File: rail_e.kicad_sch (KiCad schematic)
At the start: 49 parts

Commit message: PCBA prototype order
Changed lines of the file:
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@@
-	)
-	(junction
-		(at 279.4 123.19)
-		(diameter 0)
-		(color 0 0 0 0)
 	)
 	(junction
@@
 		)
 		(stroke
-			(width 0)
-			(type default)
-		)
-	)
-	(wire
-		(pts
-			(xy 279.4 123.19) (xy 279.4 147.32)
-		)
-		(stroke

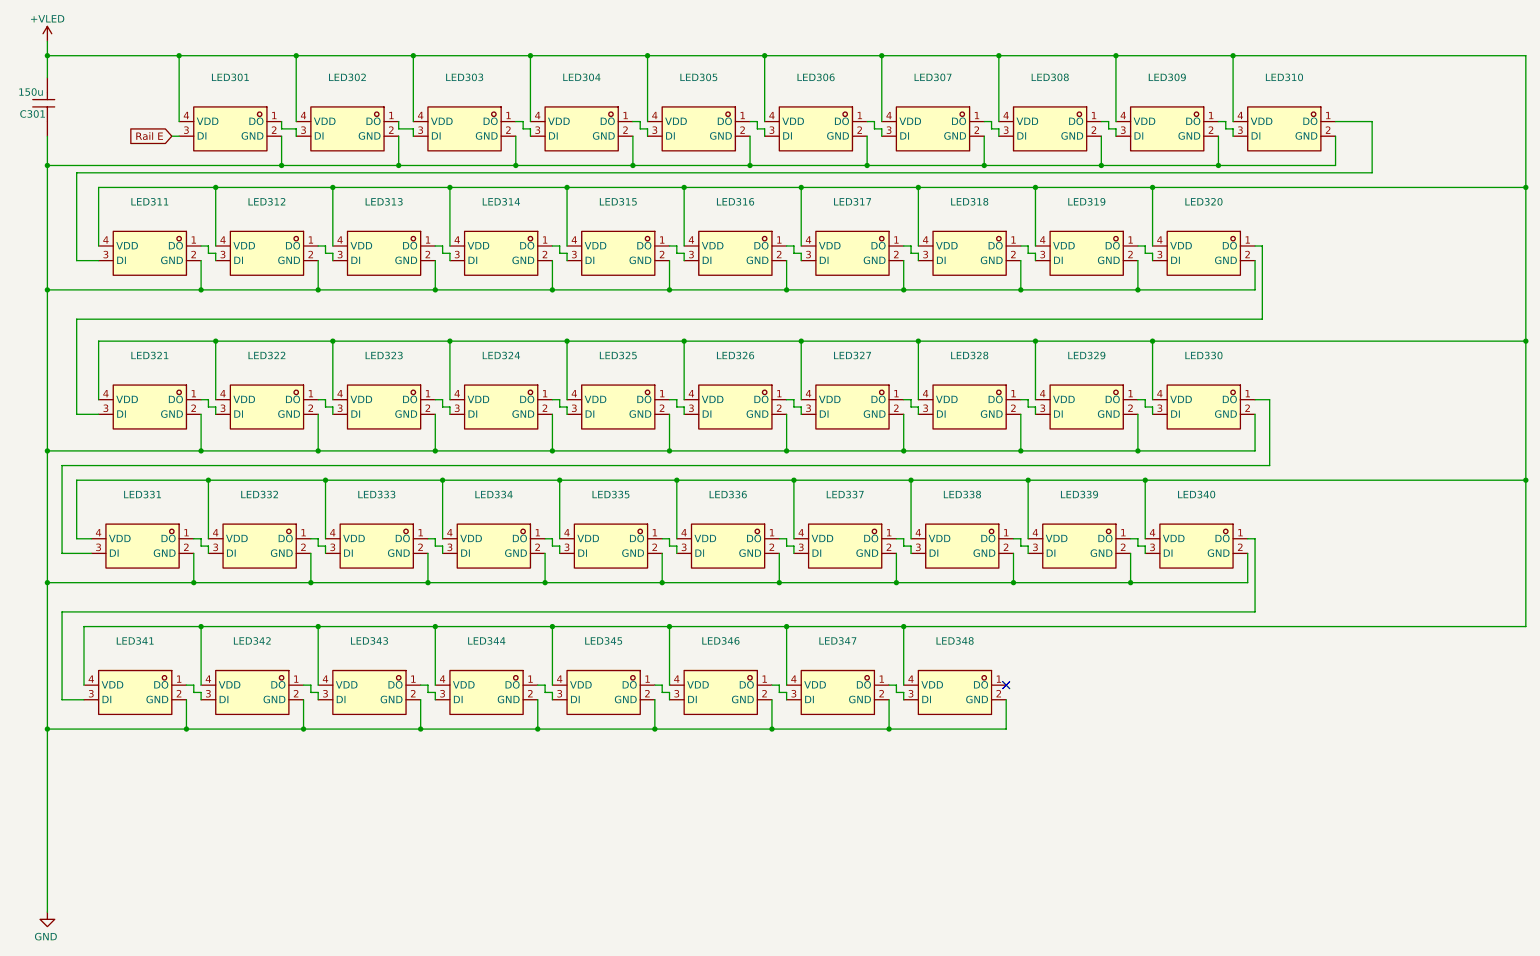
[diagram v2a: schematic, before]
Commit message: Add rail labels
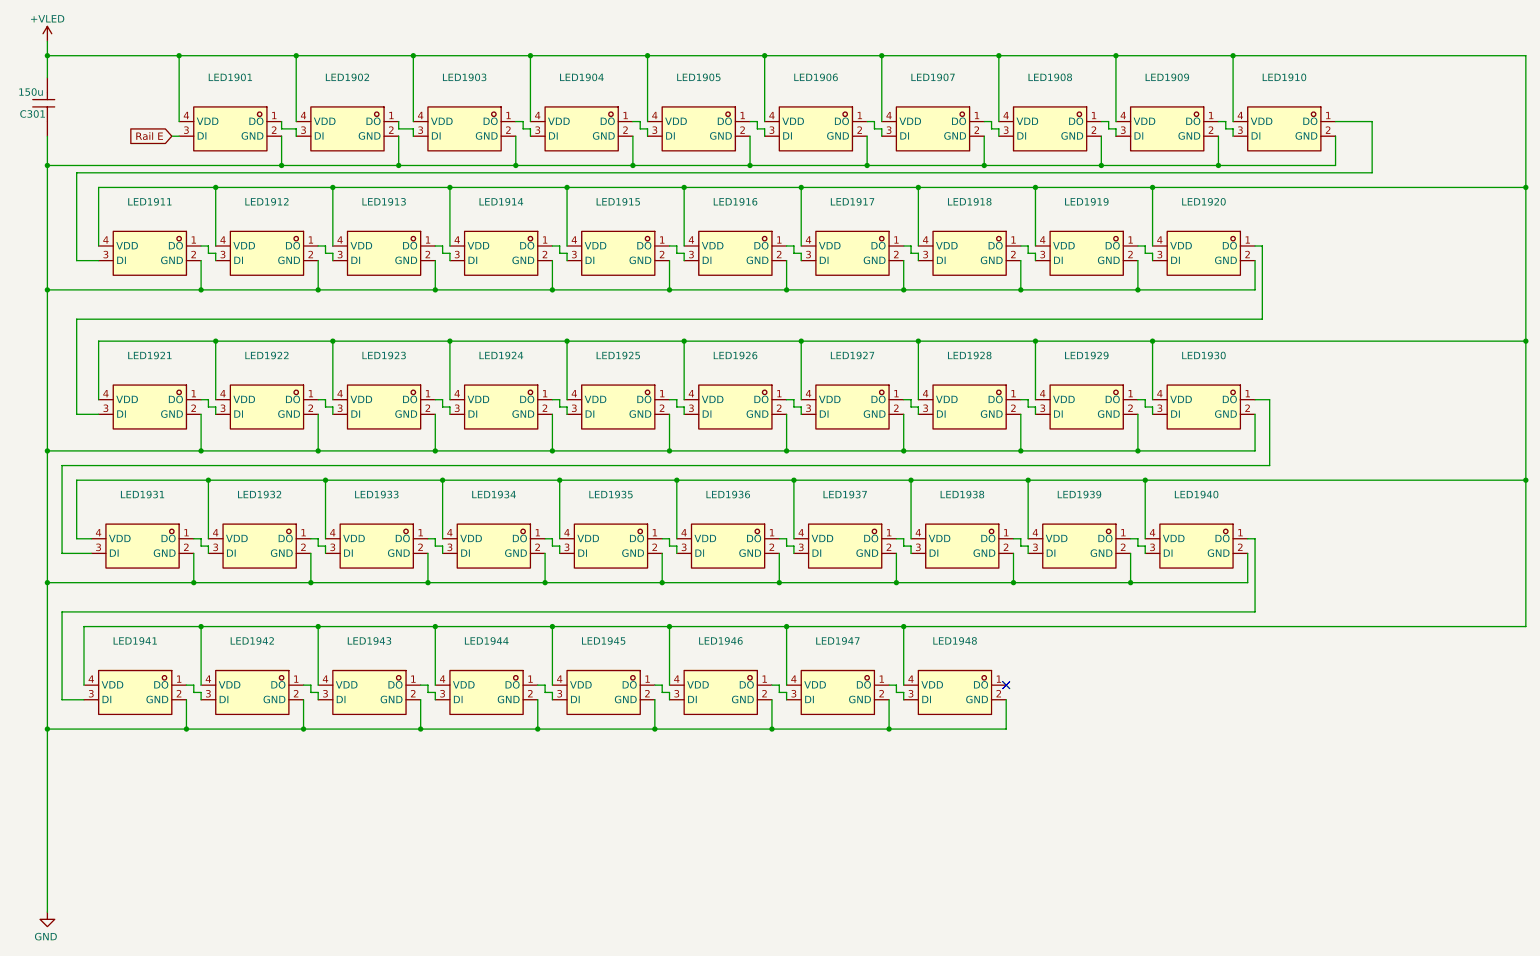
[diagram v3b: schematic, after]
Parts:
- renumbered LED301 to LED1901, LED302 to LED1902, LED303 to LED1903, LED304 to LED1904, LED305 to LED1905, LED306 to LED1906, LED307 to LED1907, LED308 to LED1908, LED309 to LED1909, LED310 to LED1910, LED311 to LED1911, LED312 to LED1912, LED313 to LED1913, LED314 to LED1914, LED315 to LED1915, LED316 to LED1916, LED317 to LED1917, LED318 to LED1918, LED319 to LED1919, LED320 to LED1920, LED321 to LED1921, LED322 to LED1922, LED323 to LED1923, LED324 to LED1924, LED325 to LED1925, LED326 to LED1926, LED327 to LED1927, LED328 to LED1928, LED329 to LED1929, LED330 to LED1930, LED331 to LED1931, LED332 to LED1932, LED333 to LED1933, LED334 to LED1934, LED335 to LED1935, LED336 to LED1936, LED337 to LED1937, LED338 to LED1938, LED339 to LED1939, LED340 to LED1940, LED341 to LED1941, LED342 to LED1942, LED343 to LED1943, LED344 to LED1944, LED345 to LED1945, LED346 to LED1946, LED347 to LED1947, LED348 to LED1948

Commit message: route T
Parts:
- renumbered LED1901 to LED1701, LED1902 to LED1702, LED1903 to LED1703, LED1904 to LED1704, LED1905 to LED1705, LED1906 to LED1706, LED1907 to LED1707, LED1908 to LED1708, LED1909 to LED1709, LED1910 to LED1710, LED1911 to LED1711, LED1912 to LED1712, LED1913 to LED1713, LED1914 to LED1714, LED1915 to LED1715, LED1916 to LED1716, LED1917 to LED1717, LED1918 to LED1718, LED1919 to LED1719, LED1920 to LED1720, LED1921 to LED1721, LED1922 to LED1722, LED1923 to LED1723, LED1924 to LED1724, LED1925 to LED1725, LED1926 to LED1726, LED1927 to LED1727, LED1928 to LED1728, LED1929 to LED1729, LED1930 to LED1730, LED1931 to LED1731, LED1932 to LED1732, LED1933 to LED1733, LED1934 to LED1734, LED1935 to LED1735, LED1936 to LED1736, LED1937 to LED1737, LED1938 to LED1738, LED1939 to LED1739, LED1940 to LED1740, LED1941 to LED1741, LED1942 to LED1742, LED1943 to LED1743, LED1944 to LED1744, LED1945 to LED1745, LED1946 to LED1746, LED1947 to LED1747, LED1948 to LED1748

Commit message: route link 1
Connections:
- net +VLED: no longer LED1742.4 (VDD)
- net at LED1742.3 (DI): no longer LED1741.1 (DO)
- net LINK_2_1: now reaches LED1748.1 (DO)
- net Rail E renamed LINK_1_2
- no-connect marks 1 -> 0
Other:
- moved on the sheet: LED1742
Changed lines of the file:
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@@
 		(color 0 0 0 0)
 	)
-	(no_connect
-		(at 189.23 133.35)
-	)
 	(wire
 		(pts
@@
 		)
 	)
-	(global_label "Rail E"
+	(global_label "LINK_1_2"
 		(shape input)
 		(at 44.45 38.1 180)
@@
 		)
 		(property "Intersheetrefs" "${INTERSHEET_REFS}"
-			(at 35.6592 38.1 0)
+			(at 32.8772 38.1 0)
 			(hide yes)
 			(show_name no)
@@
 		)
 	)
+	(global_label "LINK_2_1"
+		(shape input)
+		(at 189.23 133.35 0)
+		(fields_autoplaced yes)
+		(effects
+			(font
+				(size 1.27 1.27)
+			)
+			(justify left)
+		)
+		(property "Intersheetrefs" "${INTERSHEET_REFS}"
+			(at 200.8028 133.35 0)
+			(hide yes)
+			(show_name no)
+			(do_not_autoplace no)
+			(effects
+				(font
+					(size 1.27 1.27)
+				)
+				(justify left)
+			)
+		)
+	)
 	(symbol
 		(lib_id "power:GND")
@@
 		(lib_id "EasyEDA:WS2812B-2020")
 		(at 67.31 130.81 0)
-		(mirror y)
 		(unit 1)
 		(body_style 1)
@@
 		(dnp no)
 		(property "Reference" "LED1742"
-			(at 58.42 125.73 0)
+			(at 76.2 125.73 0)
 			(show_name no)
 			(do_not_autoplace no)
@@
 		)
 		(property "Value" "WS2812B-2020"
-			(at 58.42 128.27 0)
+			(at 76.2 128.27 0)
 			(hide yes)
 			(show_name no)

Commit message: route link 2
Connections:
- net +VLED: now also LED1742.4 (VDD)
- net at LED1742.3 (DI): now also LED1741.1 (DO)
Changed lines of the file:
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@@
 	)
 	(junction
-		(at 67.31 140.97)
-		(diameter 0)
-		(color 0 0 0 0)
-	)
-	(junction
 		(at 52.07 73.66)
 		(diameter 0)
@@
 	)
 	(junction
+		(at 67.31 140.97)
+		(diameter 0)
+		(color 0 0 0 0)
+	)
+	(junction
 		(at 147.32 24.13)
 		(diameter 0)
@@
 	(wire
 		(pts
-			(xy 69.85 59.69) (xy 69.85 64.77)
+			(xy 67.31 140.97) (xy 87.63 140.97)
 		)
 		(stroke
@@
 	(wire
 		(pts
-			(xy 67.31 135.89) (xy 67.31 140.97)
+			(xy 69.85 59.69) (xy 69.85 64.77)
 		)
 		(stroke
@@
 	(wire
 		(pts
-			(xy 67.31 133.35) (xy 68.58 133.35)
-		)
-		(stroke
-			(width 0)
-			(type default)
-		)
-	)
-	(wire
-		(pts
 			(xy 171.45 92.71) (xy 151.13 92.71)
 		)
@@
 	(wire
 		(pts
-			(xy 87.63 140.97) (xy 67.31 140.97)
-		)
-		(stroke
-			(width 0)
-			(type default)
-		)
-	)
-	(wire
-		(pts
 			(xy 214.63 58.42) (xy 214.63 59.69)
 		)
@@
 	(wire
 		(pts
+			(xy 67.31 135.89) (xy 67.31 140.97)
+		)
+		(stroke
+			(width 0)
+			(type default)
+		)
+	)
+	(wire
+		(pts
 			(xy 130.81 64.77) (xy 151.13 64.77)
 		)
@@
 	(wire
 		(pts
+			(xy 67.31 133.35) (xy 68.58 133.35)
+		)
+		(stroke
+			(width 0)
+			(type default)
+		)
+	)
+	(wire
+		(pts
 			(xy 151.13 86.36) (xy 151.13 92.71)
 		)
@@
 	(wire
 		(pts
-			(xy 67.31 140.97) (xy 46.99 140.97)
+			(xy 46.99 140.97) (xy 67.31 140.97)
 		)
 		(stroke
@@
 	(symbol
 		(lib_id "EasyEDA:WS2812B-2020")
-		(at 67.31 130.81 0)
-		(unit 1)
-		(body_style 1)
-		(exclude_from_sim no)
-		(in_bom yes)
-		(on_board yes)
-		(in_pos_files yes)
-		(dnp no)
-		(property "Reference" "LED1742"
-			(at 76.2 125.73 0)
-			(show_name no)
-			(do_not_autoplace no)
-			(effects
-				(font
-					(size 1.27 1.27)
-				)
-			)
-		)
-		(property "Value" "WS2812B-2020"
-			(at 76.2 128.27 0)
-			(hide yes)
-			(show_name no)
-			(do_not_autoplace no)
-			(effects
-				(font
-					(size 1.27 1.27)
-				)
-			)
-		)
-		(property "Footprint" "EasyEDA:LED-SMD_4P-L2.0-W2.0-TL_WS2812B-2020"
-			(at 67.31 143.51 0)
-			(hide yes)
-			(show_name no)
-			(do_not_autoplace no)
-			(effects
-				(font
-					(size 1.27 1.27)
-				)
-			)
-		)
-		(property "Datasheet" "https://lcsc.com/product-detail/Light-Emitting-Diodes-LED_Worldsemi-WS2812B-2020_C965555.html"
-			(at 67.31 146.05 0)
-			(hide yes)
-			(show_name no)
-			(do_not_autoplace no)
-			(effects
-				(font
-					(size 1.27 1.27)
-				)
-			)
-		)
-		(property "Description" ""
-			(at 67.31 130.81 0)
-			(hide yes)
-			(show_name no)
-			(do_not_autoplace no)
-			(effects
-				(font
-					(size 1.27 1.27)
-				)
-			)
-		)
-		(property "LCSC Part" "C965555"
-			(at 67.31 148.59 0)
-			(hide yes)
-			(show_name no)
-			(do_not_autoplace no)
-			(effects
-				(font
-					(size 1.27 1.27)
-				)
-			)
-		)
-		(pin "1"
-		)
-		(pin "2"
-		)
-		(pin "4"
-		)
-		(pin "3"
-		)
-		(instances
-			(project "transit"
-				(path "/3763eade-a8c8-4ec0-9cf2-9db4442b4ee5/77ee1b5c-3800-46a1-aec6-a1e3c1d3f80f/80c06a5e-cea2-47d9-b67a-41d837fcb0a2"
-					(reference "LED1742")
-					(unit 1)
-				)
-			)
-		)
-	)
-	(symbol
-		(lib_id "EasyEDA:WS2812B-2020")
 		(at 110.49 54.61 0)
 		(mirror y)
@@
 					(unit 1)
 				)
+			)
+		)
+	)
+	(symbol
+		(lib_id "EasyEDA:WS2812B-2020")
+		(at 67.31 130.81 0)
+		(mirror y)
+		(unit 1)
+		(body_style 1)
+		(exclude_from_sim no)
+		(in_bom yes)
+		(on_board yes)
+		(in_pos_files yes)
+		(dnp no)
+		(property "Reference" "LED1742"
+			(at 58.42 125.73 0)
+			(show_name no)
+			(do_not_autoplace no)
+			(effects
+				(font
+					(size 1.27 1.27)
+				)
+			)
+		)
+		(property "Value" "WS2812B-2020"
+			(at 58.42 128.27 0)
+			(hide yes)
+			(show_name no)
+			(do_not_autoplace no)
+			(effects
+				(font
+					(size 1.27 1.27)
+				)
+			)
+		)
+		(property "Footprint" "EasyEDA:LED-SMD_4P-L2.0-W2.0-TL_WS2812B-2020"
+			(at 67.31 143.51 0)
+			(hide yes)
+			(show_name no)
+			(do_not_autoplace no)
+			(effects
+				(font
+					(size 1.27 1.27)
+				)
+			)
+		)
+		(property "Datasheet" "https://lcsc.com/product-detail/Light-Emitting-Diodes-LED_Worldsemi-WS2812B-2020_C965555.html"
+			(at 67.31 146.05 0)
+			(hide yes)
+			(show_name no)
+			(do_not_autoplace no)
+			(effects
+				(font
+					(size 1.27 1.27)
+				)
+			)
+		)
+		(property "Description" ""
+			(at 67.31 130.81 0)
+			(hide yes)
+			(show_name no)
+			(do_not_autoplace no)
+			(effects
+				(font
+					(size 1.27 1.27)
+				)
+			)
+		)
+		(property "LCSC Part" "C965555"
+			(at 67.31 148.59 0)
+			(hide yes)
+			(show_name no)
+			(do_not_autoplace no)
+			(effects
+				(font
+					(size 1.27 1.27)
+				)
+			)
+		)
+		(pin "1"
+		)
+		(pin "2"
+		)
+		(pin "4"
+		)
+		(pin "3"
+		)
+		(instances
+			(project "transit"
+				(path "/3763eade-a8c8-4ec0-9cf2-9db4442b4ee5/77ee1b5c-3800-46a1-aec6-a1e3c1d3f80f/80c06a5e-cea2-47d9-b67a-41d837fcb0a2"
+					(reference "LED1742")
+					(unit 1)
+				)

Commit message: rev-b validation run
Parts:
- removed C301: 150u, EasyEDA:CAP-SMD_L3.5-W2.8, symbol EasyEDA:CL21B106KOQNNNE
- LED1701, LED1702, LED1703, LED1704, LED1705, LED1706, LED1707, LED1708, LED1709, LED1710, LED1711, LED1712, LED1713, LED1714, LED1715, LED1716, LED1717, LED1718, LED1719, LED1720, LED1721, LED1722, LED1723, LED1724, LED1725, LED1726, LED1727, LED1728, LED1729, LED1730, LED1731, LED1732, LED1733, LED1734, LED1735, LED1736, LED1737, LED1738, LED1739, LED1740, LED1741, LED1742, LED1743, LED1744, LED1745, LED1746, LED1747, LED1748: LCSC Part C965555 -> C52917434
